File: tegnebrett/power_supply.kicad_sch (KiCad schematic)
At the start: 32 parts, among them U3 TPS54325PWP, U4 TPS54294PWP

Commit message: feat: PCB update
Main additions:

- Added LEDs to Power Supply, MCU and FPGA.
The resistor values will depend on the specific LEDs we buy.
Red LEDs need a different resistor value than blue LEDs, etc.

- Added a bunch of buttons to the MCU
It doesn't hurt to have some redundancy here.

- Added header pins
Allows us to easily reach GPIO pins on the MCU and the FPGA.
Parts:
- added D1: LED, symbol Device:LED
- added R71: R, symbol Device:R
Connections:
- net +3V3: now also R71.2
- net GND: now also D1.1 (K)
- new net: D1.2 (A), R71.1

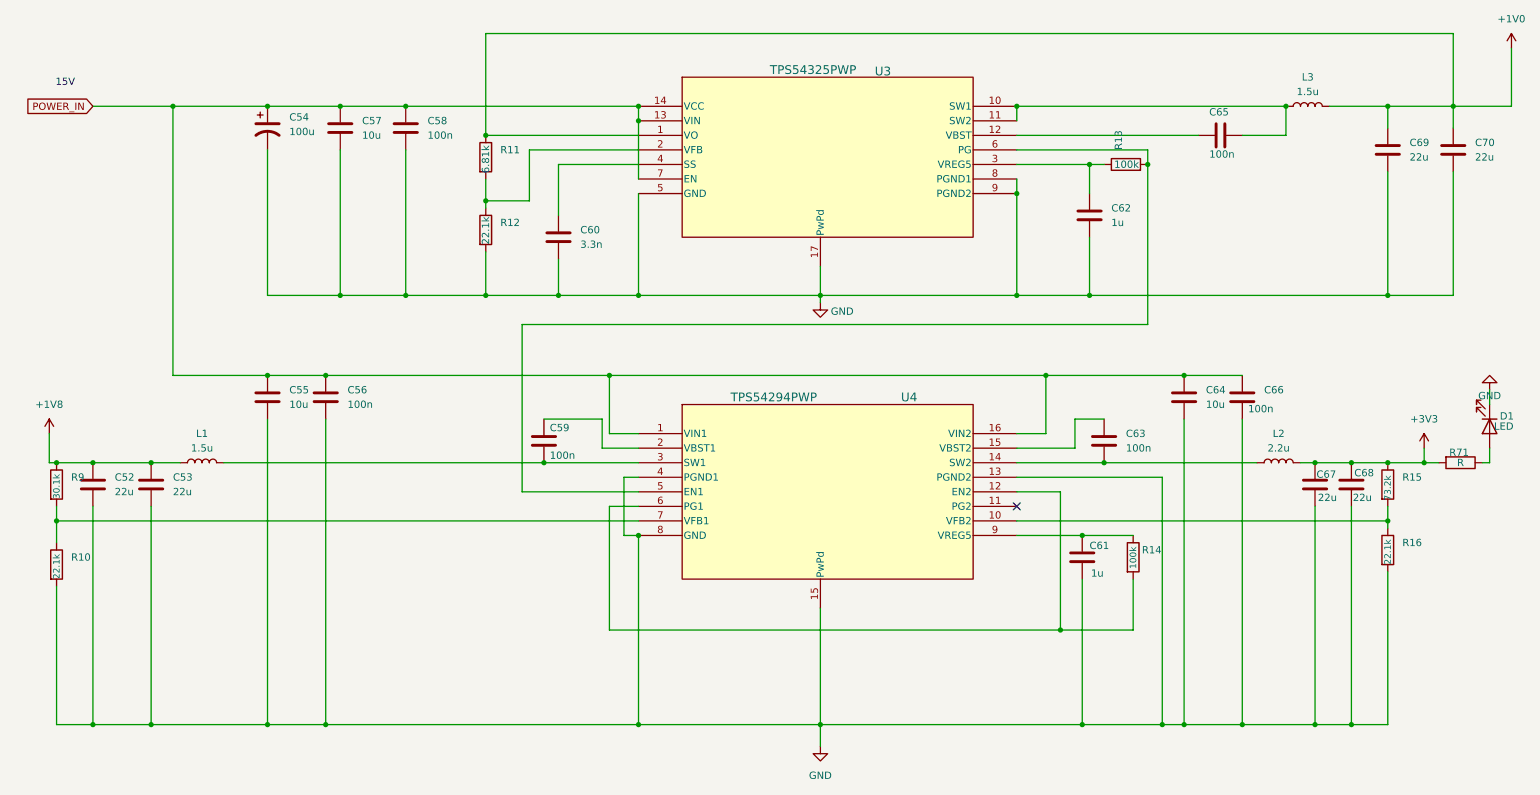
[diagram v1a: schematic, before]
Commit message: feat(PCB-schematic): add power flags
This removes a lot of the warnings we're getting from the ERC checker.
There are still some warnings on the PSU, probably because we've set the
wrong pin type on some of the pins.
For example output instead of power output, etc.
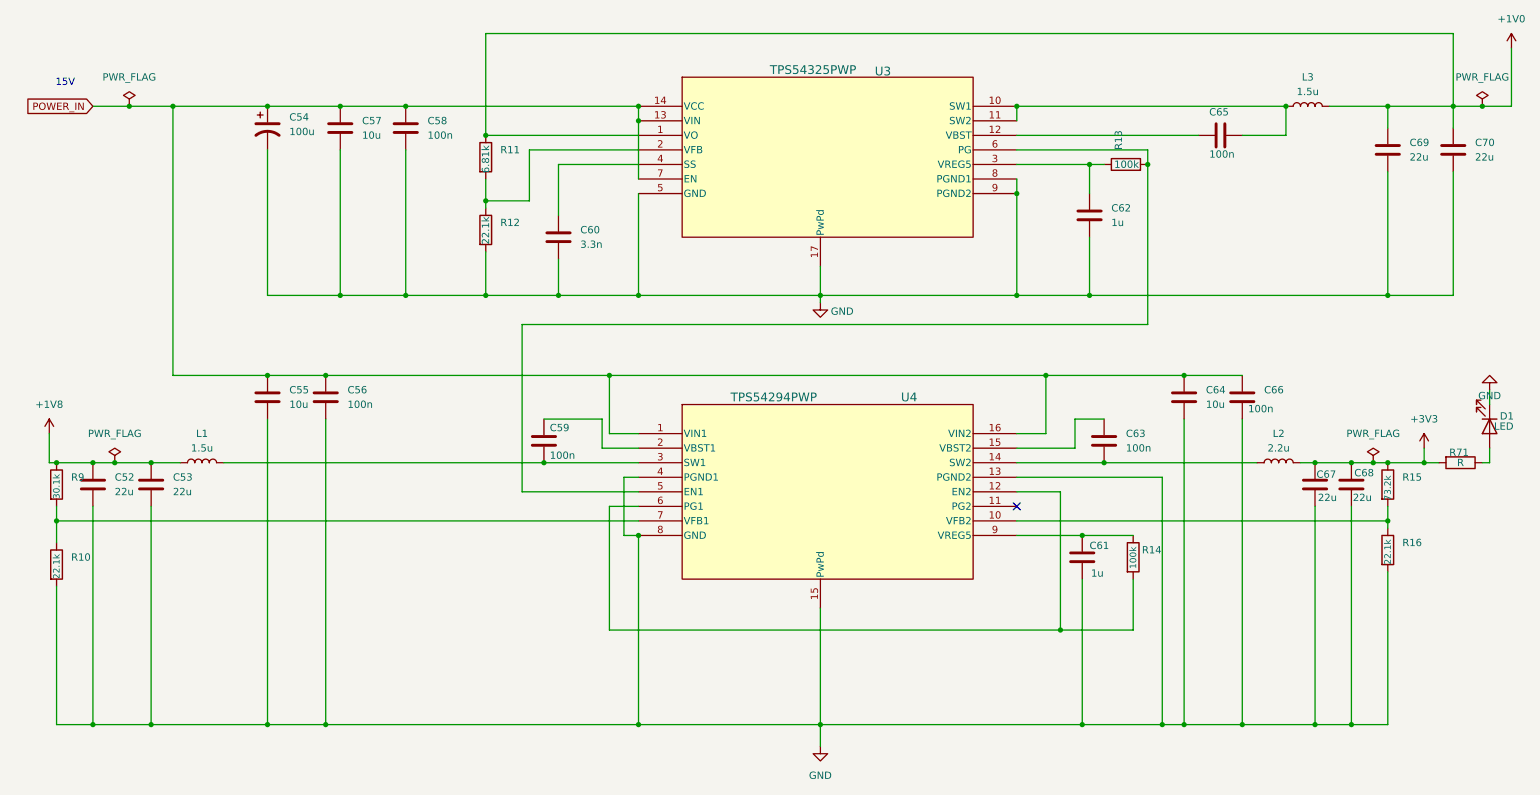
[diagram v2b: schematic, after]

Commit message: feat: add USB-A symbol and footprint to schematic
Also included the 3D model. Now there's some stuff in the PCB.
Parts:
- U3: footprint PWP14_2P31X2P46 -> (none)
- U4: footprint PWP16_2P31X2P46 -> (none)
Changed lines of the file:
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@@
 			)
 		)
-		(property "Footprint" "PWP16_2P31X2P46"
+		(property "Footprint" ""
 			(at 121.92 102.87 0)
 			(effects
@@
 			)
 		)
-		(property "Footprint" "PWP14_2P31X2P46"
+		(property "Footprint" ""
 			(at 121.92 45.72 0)
 			(effects
